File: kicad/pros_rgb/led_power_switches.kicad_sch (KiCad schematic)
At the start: 32 parts, among them Q1 N54D, Q2 N54D, Q3 N54D, Q4 N54D, Q5 N54D, Q6 N54D, Q7 N54D, Q8 N54D

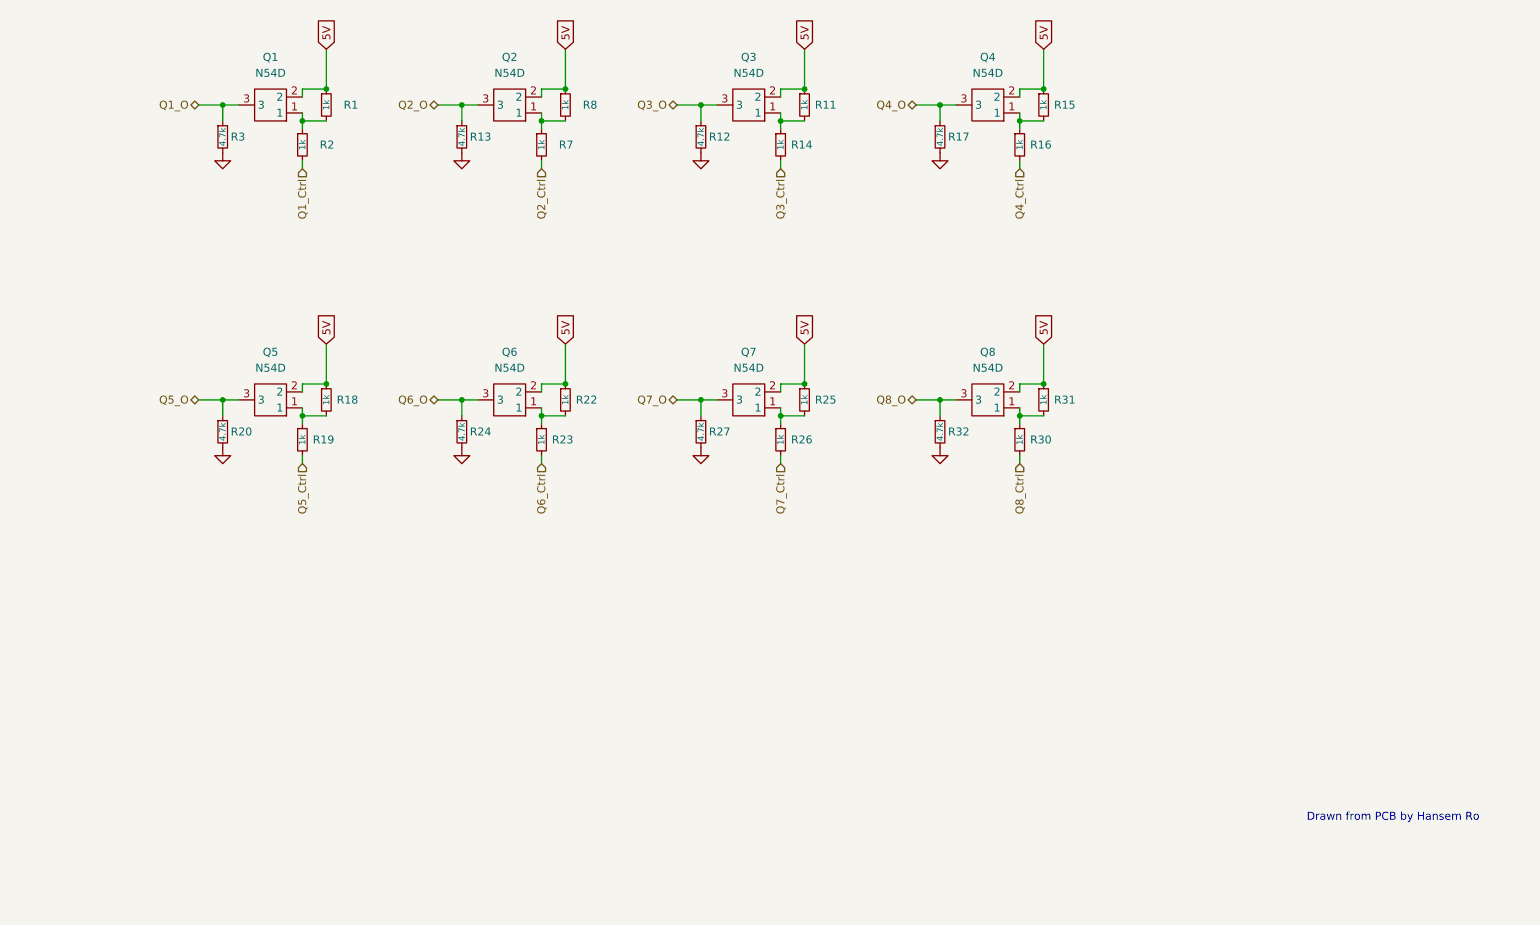
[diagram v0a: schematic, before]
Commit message: kicad/pros_rgb: use pmos symbol for N54D
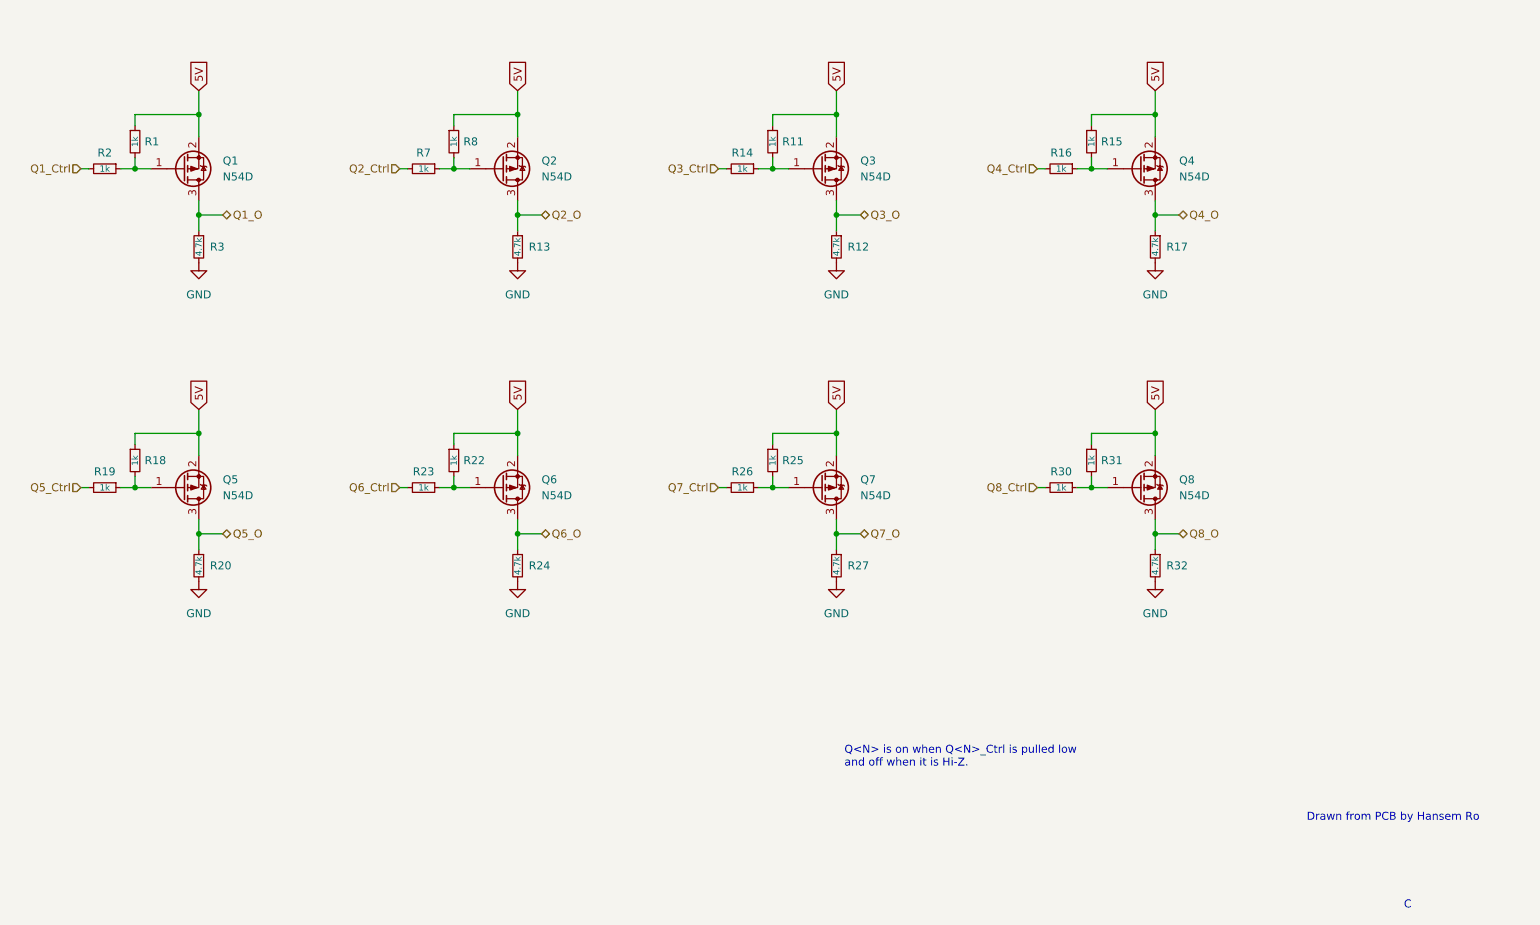
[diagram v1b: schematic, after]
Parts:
- removed Q1, Q2, Q3, Q4, Q5, Q6, Q7, Q8: N54D, symbol SMD_components:N54D
- added Q1, Q2, Q3, Q4, Q5, Q6, Q7, Q8: N54D, symbol Device:Q_PMOS_GSD
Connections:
- net 5V: now also Q1.2 (S), Q2.2 (S), Q3.2 (S), Q4.2 (S), Q5.2 (S), Q6.2 (S), Q7.2 (S), Q8.2 (S)
- net Q1_O: now also Q1.3 (D)
- net Q2_O: now also Q2.3 (D)
- net Q3_O: now also Q3.3 (D)
- net Q4_O: now also Q4.3 (D)
- net Q5_O: now also Q5.3 (D)
- net Q6_O: now also Q6.3 (D)
- net Q7_O: now also Q7.3 (D)
- net Q8_O: now also Q8.3 (D)
- net at R1.2, R2.1: now also Q1.1 (G)
- net at R15.2, R16.1: now also Q4.1 (G)
- net at R11.2, R14.1: now also Q3.1 (G)
- net at R30.1, R31.2: now also Q8.1 (G)
- net at R18.2, R19.1: now also Q5.1 (G)
- net at R7.1, R8.2: now also Q2.1 (G)
- net at R22.2, R23.1: now also Q6.1 (G)
- net at R25.2, R26.1: now also Q7.1 (G)
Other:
- note added: "C"
- note added: "Q<N> is on when Q<N>_Ctrl is pulled low and off when it is Hi-Z."
